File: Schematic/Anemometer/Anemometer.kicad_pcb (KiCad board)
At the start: 2 copper layers, 35 x 91 mm, 9 parts, among them J1 Battery, J2 Screen, J3 CG_Anem, U1 TP4065_ChargeModule, U2 MCP1700x-330xxTO, U3 WeMos_D1_mini

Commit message: Case  and PCB Fixes
Правки сборки после перевода на стаб MCP1700.
Вместо полных вырезов для USB сделаны выемки.  Их достаточно.
Передвинут разъем к сенсору на PCB, иначе провода загибаются прям впритирку к корпусу.
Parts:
- moved J3 3.55 mm to (184.5, 76.0)
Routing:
- net Net-(C2-Pad1): track 104.4 -> 100.2 mm
- net Net-(C1-Pad1): track 97.8 -> 101.5 mm
- net Net-(J2-Pad4): track 62.9 -> 59.8 mm
- net Net-(J2-Pad3): track 59.5 -> 56.3 mm
- net GND: track 70.9 -> 67.8 mm
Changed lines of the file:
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@@
   )
   (footprint "Connector_JST:JST_EH_S4B-EH_1x04_P2.50mm_Horizontal" (layer "F.Cu")
-    (at 185.25 72.5325)
+    (at 184.5 76)
     (descr "JST EH series connector, S4B-EH (http://www.jst-mfg.com/product/pdf/eng/eEH.pdf), generated with kicad-footprint-generator")
     (tags "connector JST EH horizontal")
@@
   (gr_line locked (start 165 65) (end 169 65) (layer "Edge.Cuts") (width 0.2))
   (segment (start 170.25 118.75) (end 168 121) (width 0.8) (layer "F.Cu") (net 1))
-  (segment (start 177.75 75.75) (end 181.25 79.25) (width 0.8) (layer "F.Cu") (net 1))
   (segment (start 188.73 92) (end 188.73 90.48) (width 0.8) (layer "F.Cu") (net 1))
   (segment (start 168 124.5) (end 169.04 125.54) (width 0.8) (layer "F.Cu") (net 1))
+  (segment (start 174 67.75) (end 172.17 67.75) (width 0.8) (layer "F.Cu") (net 1))
+  (segment (start 177.5 71.25) (end 174 67.75) (width 0.8) (layer "F.Cu") (net 1))
   (segment (start 169.04 125.54) (end 171 125.54) (width 0.8) (layer "F.Cu") (net 1))
   (segment (start 170 126) (end 170.54 126) (width 0.25) (layer "F.Cu") (net 1))
-  (segment (start 177.75 73.33) (end 177.75 73.75) (width 0.4) (layer "F.Cu") (net 1))
-  (segment (start 186.75 79.25) (end 187.05 79.55) (width 0.4) (layer "F.Cu") (net 1))
+  (segment (start 187.05 82.7) (end 187.05 87) (width 0.8) (layer "F.Cu") (net 1))
   (segment (start 170.25 69.67) (end 170.25 118.75) (width 0.8) (layer "F.Cu") (net 1))
-  (segment (start 172.17 67.75) (end 177.75 73.33) (width 0.8) (layer "F.Cu") (net 1))
-  (segment (start 187.05 79.55) (end 187.05 87) (width 0.8) (layer "F.Cu") (net 1))
-  (segment (start 177.75 73.75) (end 177.75 75.75) (width 0.8) (layer "F.Cu") (net 1))
+  (segment (start 181.75 82.5) (end 181.75 79.75) (width 0.8) (layer "F.Cu") (net 1))
   (segment (start 168 121) (end 168 124.5) (width 0.8) (layer "F.Cu") (net 1))
   (segment (start 188.73 90.48) (end 187 88.75) (width 0.8) (layer "F.Cu") (net 1))
   (segment (start 172.17 67.75) (end 170.25 69.67) (width 0.8) (layer "F.Cu") (net 1))
+  (segment (start 177.5 75.5) (end 177.5 71.25) (width 0.8) (layer "F.Cu") (net 1))
+  (segment (start 181.75 79.75) (end 177.5 75.5) (width 0.8) (layer "F.Cu") (net 1))
   (segment (start 187 87.05) (end 187.05 87) (width 0.4) (layer "F.Cu") (net 1))
   (segment (start 187 88.75) (end 187 87.05) (width 0.8) (layer "F.Cu") (net 1))
   (segment (start 170.54 126) (end 171 125.54) (width 0.25) (layer "F.Cu") (net 1))
-  (via (at 181.25 79.25) (size 2) (drill 0.8) (layers "F.Cu" "B.Cu") (net 1))
-  (via (at 186.75 79.25) (size 2) (drill 0.8) (layers "F.Cu" "B.Cu") (net 1))
-  (segment (start 181.25 79.25) (end 186.75 79.25) (width 0.4) (layer "B.Cu") (net 1))
-  (segment (start 187 79.5) (end 186.75 79.25) (width 0.4) (layer "B.Cu") (net 1))
+  (via (at 181.75 82.5) (size 2) (drill 0.8) (layers "F.Cu" "B.Cu") (net 1))
+  (via (at 187.05 82.7) (size 2) (drill 0.8) (layers "F.Cu" "B.Cu") (net 1))
+  (segment (start 187.05 82.7) (end 186.85 82.5) (width 0.4) (layer "B.Cu") (net 1))
+  (segment (start 186.85 82.5) (end 181.75 82.5) (width 0.4) (layer "B.Cu") (net 1))
+  (segment (start 187.05 79.55) (end 187.05 82.7) (width 0.4) (layer "B.Cu") (net 1))
+  (segment (start 187 79.5) (end 187.05 79.55) (width 0.4) (layer "B.Cu") (net 1))
+  (segment (start 190 82) (end 187 79) (width 0.8) (layer "F.Cu") (net 2))
+  (segment (start 190 87) (end 190 82) (width 0.8) (layer "F.Cu") (net 2))
   (segment (start 191.67 115.83) (end 191.67 111) (width 0.8) (layer "F.Cu") (net 2))
   (segment (start 189.755 136.005) (end 192 138.25) (width 0.8) (layer "F.Cu") (net 2))
@@
   (segment (start 190 96.525) (end 190 92) (width 0.8) (layer "F.Cu") (net 2))
   (segment (start 190.475 97) (end 190 96.525) (width 0.4) (layer "F.Cu") (net 2))
-  (segment (start 187.75 76.5) (end 187.75 72.5325) (width 0.8) (layer "F.Cu") (net 2))
   (segment (start 192.01 138.24) (end 193.86 138.24) (width 0.8) (layer "F.Cu") (net 2))
-  (segment (start 190 87) (end 190 78.75) (width 0.8) (layer "F.Cu") (net 2))
   (segment (start 190 92) (end 190 87) (width 0.8) (layer "F.Cu") (net 2))
   (segment (start 192 138.25) (end 192.01 138.24) (width 0.4) (layer "F.Cu") (net 2))
@@
   (segment (start 189.755 124.145) (end 189.755 136.005) (width 0.8) (layer "F.Cu") (net 2))
   (segment (start 189.755 124.145) (end 189.75 124.14) (width 0.4) (layer "F.Cu") (net 2))
-  (segment (start 190 78.75) (end 187.75 76.5) (width 0.8) (layer "F.Cu") (net 2))
   (segment (start 191.67 98.195) (end 190.475 97) (width 0.8) (layer "F.Cu") (net 2))
+  (segment (start 187 79) (end 187 76) (width 0.8) (layer "F.Cu") (net 2))
   (segment (start 191.67 111) (end 191.67 98.195) (width 0.8) (layer "F.Cu") (net 2))
   (segment (start 173 139.75) (end 173 93.25) (width 0.8) (layer "F.Cu") (net 3))
-  (segment (start 184 90.5) (end 185.5 92) (width 0.8) (layer "F.Cu") (net 3))
   (segment (start 187.525 97) (end 189.13 98.605) (width 0.8) (layer "F.Cu") (net 3))
   (segment (start 185.5 92) (end 187.46 92) (width 0.8) (layer "F.Cu") (net 3))
-  (segment (start 185.25 72.5325) (end 184 73.7825) (width 0.8) (layer "F.Cu") (net 3))
   (segment (start 171 140.78) (end 171.97 140.78) (width 0.4) (layer "F.Cu") (net 3))
+  (segment (start 184.5 76) (end 184.5 91) (width 0.8) (layer "F.Cu") (net 3))
   (segment (start 171.97 140.78) (end 173 139.75) (width 0.8) (layer "F.Cu") (net 3))
   (segment (start 189.13 98.605) (end 189.13 111) (width 0.8) (layer "F.Cu") (net 3))
   (segment (start 184 93.5) (end 184.025 93.5) (width 0.4) (layer "F.Cu") (net 3))
-  (segment (start 184 73.7825) (end 184 90.5) (width 0.8) (layer "F.Cu") (net 3))
+  (segment (start 184.5 91) (end 185.5 92) (width 0.8) (layer "F.Cu") (net 3))
   (segment (start 184.025 93.5) (end 187.525 97) (width 0.8) (layer "F.Cu") (net 3))
   (segment (start 184 93.5) (end 185.5 92) (width 0.8) (layer "F.Cu") (net 3))
@@
   (segment (start 196.25 122.25) (end 194.21 120.21) (width 0.8) (layer "F.Cu") (net 6))
   (segment (start 193.86 128.08) (end 194.67 128.08) (width 0.4) (layer "F.Cu") (net 6))
-  (segment (start 193 108.25) (end 193 79) (width 0.8) (layer "F.Cu") (net 6))
+  (segment (start 193 108.25) (end 193 82) (width 0.8) (layer "F.Cu") (net 6))
+  (segment (start 194.21 109.46) (end 193 108.25) (width 0.8) (layer "F.Cu") (net 6))
   (segment (start 194.21 111) (end 194.21 109.46) (width 0.8) (layer "F.Cu") (net 6))
+  (segment (start 193 82) (end 189.5 78.5) (width 0.8) (layer "F.Cu") (net 6))
   (segment (start 194.67 128.08) (end 196.25 126.5) (width 0.8) (layer "F.Cu") (net 6))
-  (segment (start 190.25 76.25) (end 190.25 72.5325) (width 0.8) (layer "F.Cu") (net 6))
   (segment (start 194.21 120.21) (end 194.21 111) (width 0.8) (layer "F.Cu") (net 6))
-  (segment (start 193 79) (end 190.25 76.25) (width 0.8) (layer "F.Cu") (net 6))
-  (segment (start 194.21 109.46) (end 193 108.25) (width 0.8) (layer "F.Cu") (net 6))
+  (segment (start 189.5 78.5) (end 189.5 76) (width 0.8) (layer "F.Cu") (net 6))
   (segment (start 196 119.25) (end 196 111.75) (width 0.8) (layer "F.Cu") (net 7))
+  (segment (start 196.25 109.5) (end 195.65 108.9) (width 0.8) (layer "F.Cu") (net 7))
+  (segment (start 194.38 130.62) (end 198 127) (width 0.8) (layer "F.Cu") (net 7))
+  (segment (start 195.65 108.9) (end 195.627208 108.9) (width 0.8) (layer "F.Cu") (net 7))
   (segment (start 195.627208 108.9) (end 194.75 108.022792) (width 0.8) (layer "F.Cu") (net 7))
-  (segment (start 194.75 77.25) (end 192.75 75.25) (width 0.8) (layer "F.Cu") (net 7))
-  (segment (start 194.38 130.62) (end 198 127) (width 0.8) (layer "F.Cu") (net 7))
-  (segment (start 196.25 109.5) (end 195.65 108.9) (width 0.8) (layer "F.Cu") (net 7))
-  (segment (start 195.65 108.9) (end 195.627208 108.9) (width 0.8) (layer "F.Cu") (net 7))
   (segment (start 198 127) (end 198 121.25) (width 0.8) (layer "F.Cu") (net 7))
+  (segment (start 196.25 110.5) (end 196.25 109.5) (width 0.8) (layer "F.Cu") (net 7))
   (segment (start 193.86 130.62) (end 194.38 130.62) (width 0.4) (layer "F.Cu") (net 7))
-  (segment (start 196.25 110.5) (end 196.25 109.5) (width 0.8) (layer "F.Cu") (net 7))
+  (segment (start 192 77.75) (end 192 76) (width 0.8) (layer "F.Cu") (net 7))
   (segment (start 196 111.75) (end 196.75 111) (width 0.4) (layer "F.Cu") (net 7))
-  (segment (start 192.75 75.25) (end 192.75 72.5325) (width 0.8) (layer "F.Cu") (net 7))
-  (segment (start 194.75 108.022792) (end 194.75 77.25) (width 0.8) (layer "F.Cu") (net 7))
   (segment (start 196.75 111) (end 196.25 110.5) (width 0.4) (layer "F.Cu") (net 7))
+  (segment (start 194.75 80.5) (end 192 77.75) (width 0.8) (layer "F.Cu") (net 7))
+  (segment (start 194.75 108.022792) (end 194.75 80.5) (width 0.8) (layer "F.Cu") (net 7))
   (segment (start 198 121.25) (end 196 119.25) (width 0.8) (layer "F.Cu") (net 7))
   (segment (start 172.17 87.42) (end 172.17 72.83) (width 0.8) (layer "F.Cu") (net 8))

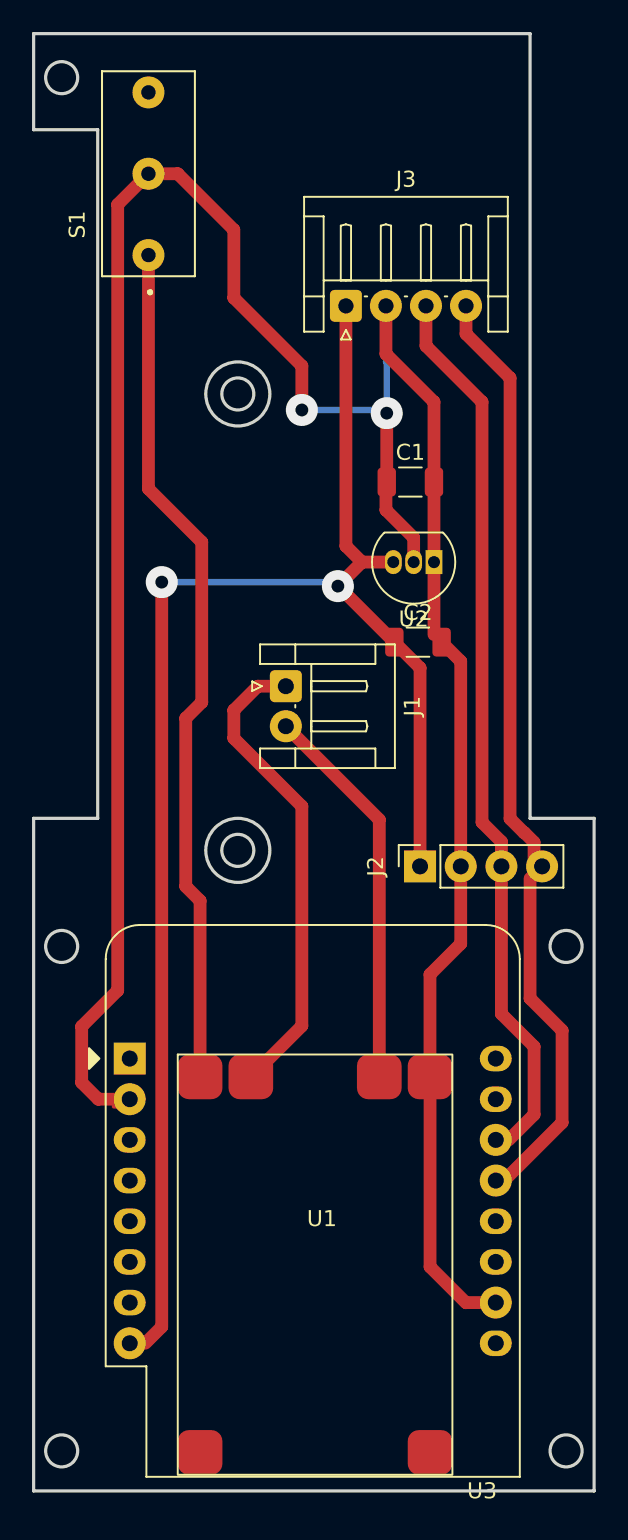
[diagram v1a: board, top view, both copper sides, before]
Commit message: Added PCB 3D model
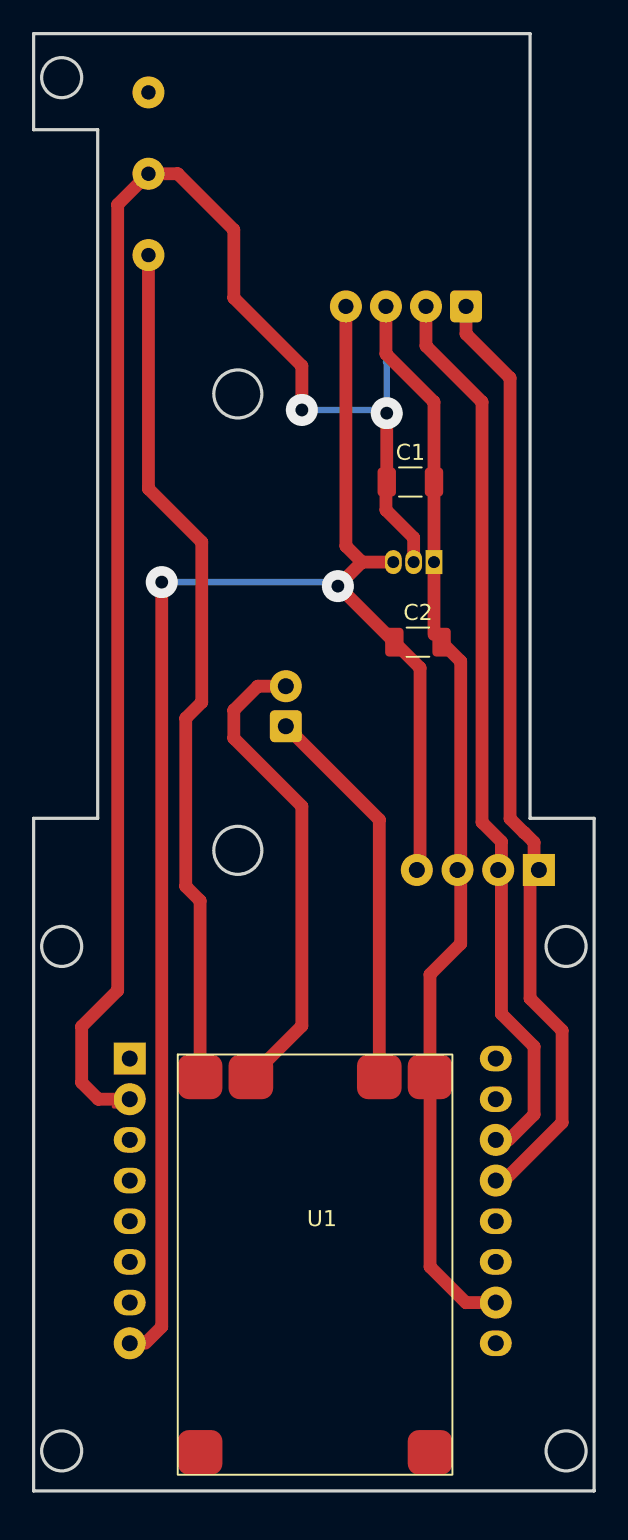
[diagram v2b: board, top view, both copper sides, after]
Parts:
- J1, J2, J3, S1, U2, U3: moved to B.Cu
- moved U3 22.0 mm to (193.0, 123.0), turned to 180 degrees
- moved J3 7.50 mm to (192.0, 76.0), turned to 180 degrees
- moved J2 7.42 mm to (196.6, 111.2)
- moved J1 2.50 mm to (180.8, 102.2), turned to 90 degrees
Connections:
- J1 pad 1: Net-(J1-Pad1) -> Net-(U1-Pad5)
- J1 pad 2: Net-(J1-Pad2) -> Net-(U1-Pad4)
- J2 pad 1: Net-(C2-Pad1) -> Net-(J2-Pad1)
- J2 pad 2: GND -> Net-(J2-Pad2)
- J2 pad 3: Net-(J2-Pad3) -> GND
- J2 pad 4: Net-(J2-Pad4) -> Net-(C2-Pad1)
- J3 pad 1: Net-(C2-Pad1) -> Net-(J2-Pad1)
- J3 pad 2: GND -> Net-(J2-Pad2)
- J3 pad 3: Net-(J2-Pad3) -> GND
- J3 pad 4: Net-(J2-Pad4) -> Net-(C2-Pad1)
- U1 pad 4: Net-(J1-Pad1) -> Net-(U1-Pad4)
- U1 pad 5: Net-(J1-Pad2) -> Net-(U1-Pad5)
- U3 pad 13: Net-(J2-Pad4) -> Net-(J2-Pad1)
- U3 pad 14: Net-(J2-Pad3) -> Net-(J2-Pad2)
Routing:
- net Net-(J2-Pad4): track 59.8 -> 0.00 mm
- net Net-(J2-Pad1): track 0.00 -> 59.8 mm
- net Net-(J2-Pad3): track 56.3 -> 0.00 mm
- net Net-(J2-Pad2): track 0.00 -> 56.3 mm
- net Net-(U1-Pad4): track 0.00 -> 29.8 mm
- net Net-(J1-Pad1): track 29.8 -> 0.00 mm
- net Net-(U1-Pad5): track 0.00 -> 24.3 mm
- net Net-(J1-Pad2): track 24.3 -> 0.00 mm
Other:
- outline, holes or cut-outs redrawn

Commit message: PCB Updated
Перемычка мешала слайдеру
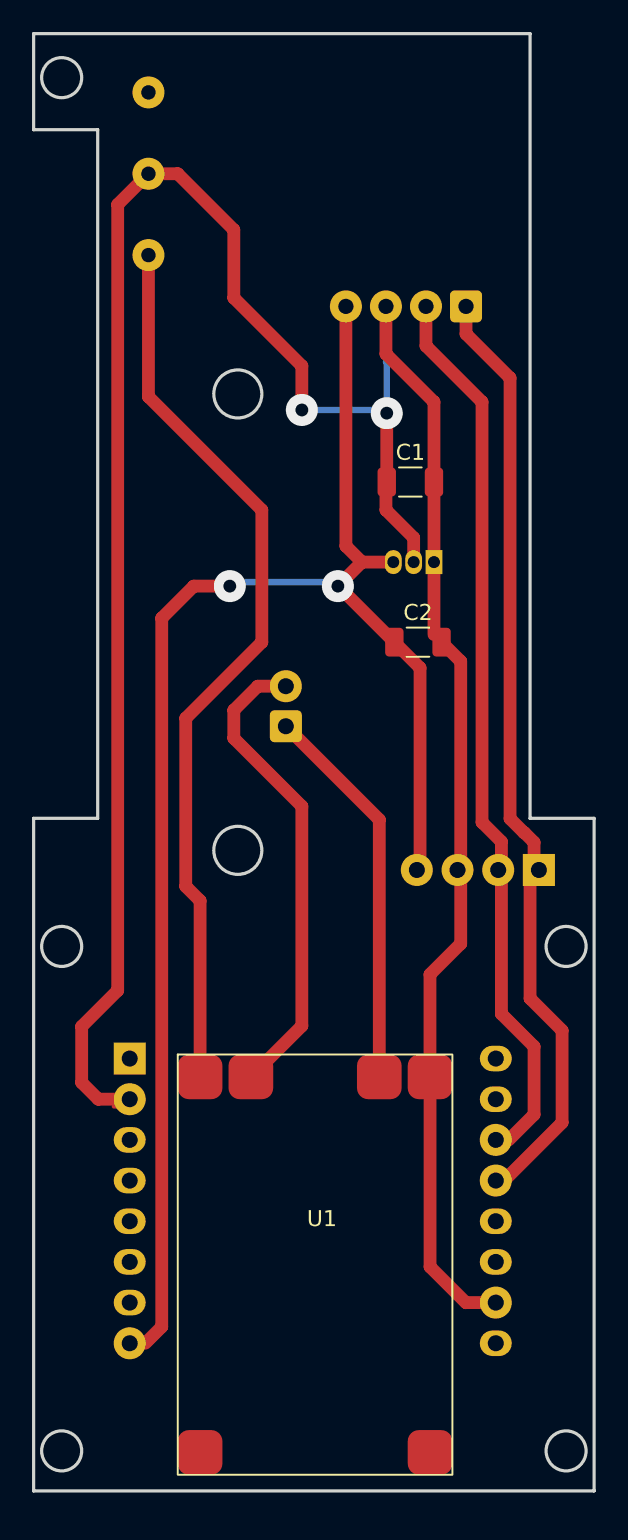
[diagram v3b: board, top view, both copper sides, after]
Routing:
- net Net-(S1-PadCOM): track 53.5 -> 56.6 mm
- net Net-(C2-Pad1): track 100.2 -> 98.8 mm
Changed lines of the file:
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@@
   (segment (start 187 79) (end 187 76) (width 0.8) (layer "F.Cu") (net 2))
   (segment (start 191.67 111) (end 191.67 98.195) (width 0.8) (layer "F.Cu") (net 2))
-  (segment (start 173 139.75) (end 173 93.25) (width 0.8) (layer "F.Cu") (net 3))
   (segment (start 187.525 97) (end 189.13 98.605) (width 0.8) (layer "F.Cu") (net 3))
   (segment (start 185.5 92) (end 187.46 92) (width 0.8) (layer "F.Cu") (net 3))
+  (segment (start 175 93.5) (end 173 95.5) (width 0.8) (layer "F.Cu") (net 3))
   (segment (start 171 140.78) (end 171.97 140.78) (width 0.4) (layer "F.Cu") (net 3))
   (segment (start 184.5 76) (end 184.5 91) (width 0.8) (layer "F.Cu") (net 3))
-  (segment (start 171.97 140.78) (end 173 139.75) (width 0.8) (layer "F.Cu") (net 3))
+  (segment (start 173 139.75) (end 171.97 140.78) (width 0.8) (layer "F.Cu") (net 3))
   (segment (start 189.13 98.605) (end 189.13 111) (width 0.8) (layer "F.Cu") (net 3))
   (segment (start 184 93.5) (end 184.025 93.5) (width 0.4) (layer "F.Cu") (net 3))
+  (segment (start 173 95.5) (end 173 139.75) (width 0.8) (layer "F.Cu") (net 3))
+  (segment (start 177.25 93.5) (end 175 93.5) (width 0.8) (layer "F.Cu") (net 3))
   (segment (start 184.5 91) (end 185.5 92) (width 0.8) (layer "F.Cu") (net 3))
   (segment (start 184.025 93.5) (end 187.525 97) (width 0.8) (layer "F.Cu") (net 3))
   (segment (start 184 93.5) (end 185.5 92) (width 0.8) (layer "F.Cu") (net 3))
   (via (at 184 93.5) (size 2) (drill 0.8) (layers "F.Cu" "B.Cu") (net 3))
-  (via (at 173 93.25) (size 2) (drill 0.8) (layers "F.Cu" "B.Cu") (net 3))
+  (via (at 177.25 93.5) (size 2) (drill 0.8) (layers "F.Cu" "B.Cu") (net 3))
+  (segment (start 177.25 93.5) (end 177.5 93.25) (width 0.4) (layer "B.Cu") (net 3))
   (segment (start 183.75 93.25) (end 184 93.5) (width 0.4) (layer "B.Cu") (net 3))
-  (segment (start 173 93.25) (end 183.75 93.25) (width 0.4) (layer "B.Cu") (net 3))
+  (segment (start 177.5 93.25) (end 183.75 93.25) (width 0.4) (layer "B.Cu") (net 3))
   (segment (start 180.75 102.25) (end 186.585 108.085) (width 0.8) (layer "F.Cu") (net 4))
   (segment (start 186.585 108.085) (end 186.585 124.145) (width 0.8) (layer "F.Cu") (net 4))
@@
   (segment (start 194.75 108.022792) (end 194.75 80.5) (width 0.8) (layer "F.Cu") (net 7))
   (segment (start 198 121.25) (end 196 119.25) (width 0.8) (layer "F.Cu") (net 7))
-  (segment (start 172.17 87.42) (end 172.17 72.83) (width 0.8) (layer "F.Cu") (net 8))
+  (segment (start 174.5 101.75) (end 179.25 97) (width 0.8) (layer "F.Cu") (net 8))
+  (segment (start 172.17 81.67) (end 172.17 72.83) (width 0.8) (layer "F.Cu") (net 8))
+  (segment (start 175.395 124.145) (end 175.395 113.145) (width 0.8) (layer "F.Cu") (net 8))
+  (segment (start 175.395 113.145) (end 174.5 112.25) (width 0.8) (layer "F.Cu") (net 8))
   (segment (start 174.5 112.25) (end 174.5 101.75) (width 0.8) (layer "F.Cu") (net 8))
-  (segment (start 174.5 101.75) (end 175.5 100.75) (width 0.8) (layer "F.Cu") (net 8))
-  (segment (start 175.395 124.145) (end 175.395 113.145) (width 0.8) (layer "F.Cu") (net 8))
-  (segment (start 175.5 100.75) (end 175.5 90.75) (width 0.8) (layer "F.Cu") (net 8))
-  (segment (start 175.395 113.145) (end 174.5 112.25) (width 0.8) (layer "F.Cu") (net 8))
-  (segment (start 175.5 90.75) (end 172.17 87.42) (width 0.8) (layer "F.Cu") (net 8))
+  (segment (start 179.25 97) (end 179.25 88.75) (width 0.8) (layer "F.Cu") (net 8))
+  (segment (start 179.25 88.75) (end 172.17 81.67) (width 0.8) (layer "F.Cu") (net 8))
 )
